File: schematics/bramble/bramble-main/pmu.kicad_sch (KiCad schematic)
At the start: 19 parts, among them J1 Conn_01x05_Pin, J7 PMU SUPPLY, J8 MAIN SUPPLY, SW1 STM_RESET, U2 STM32L031F6P6TR, U3 MCP1700x-120xxMB, Y1 Crystal

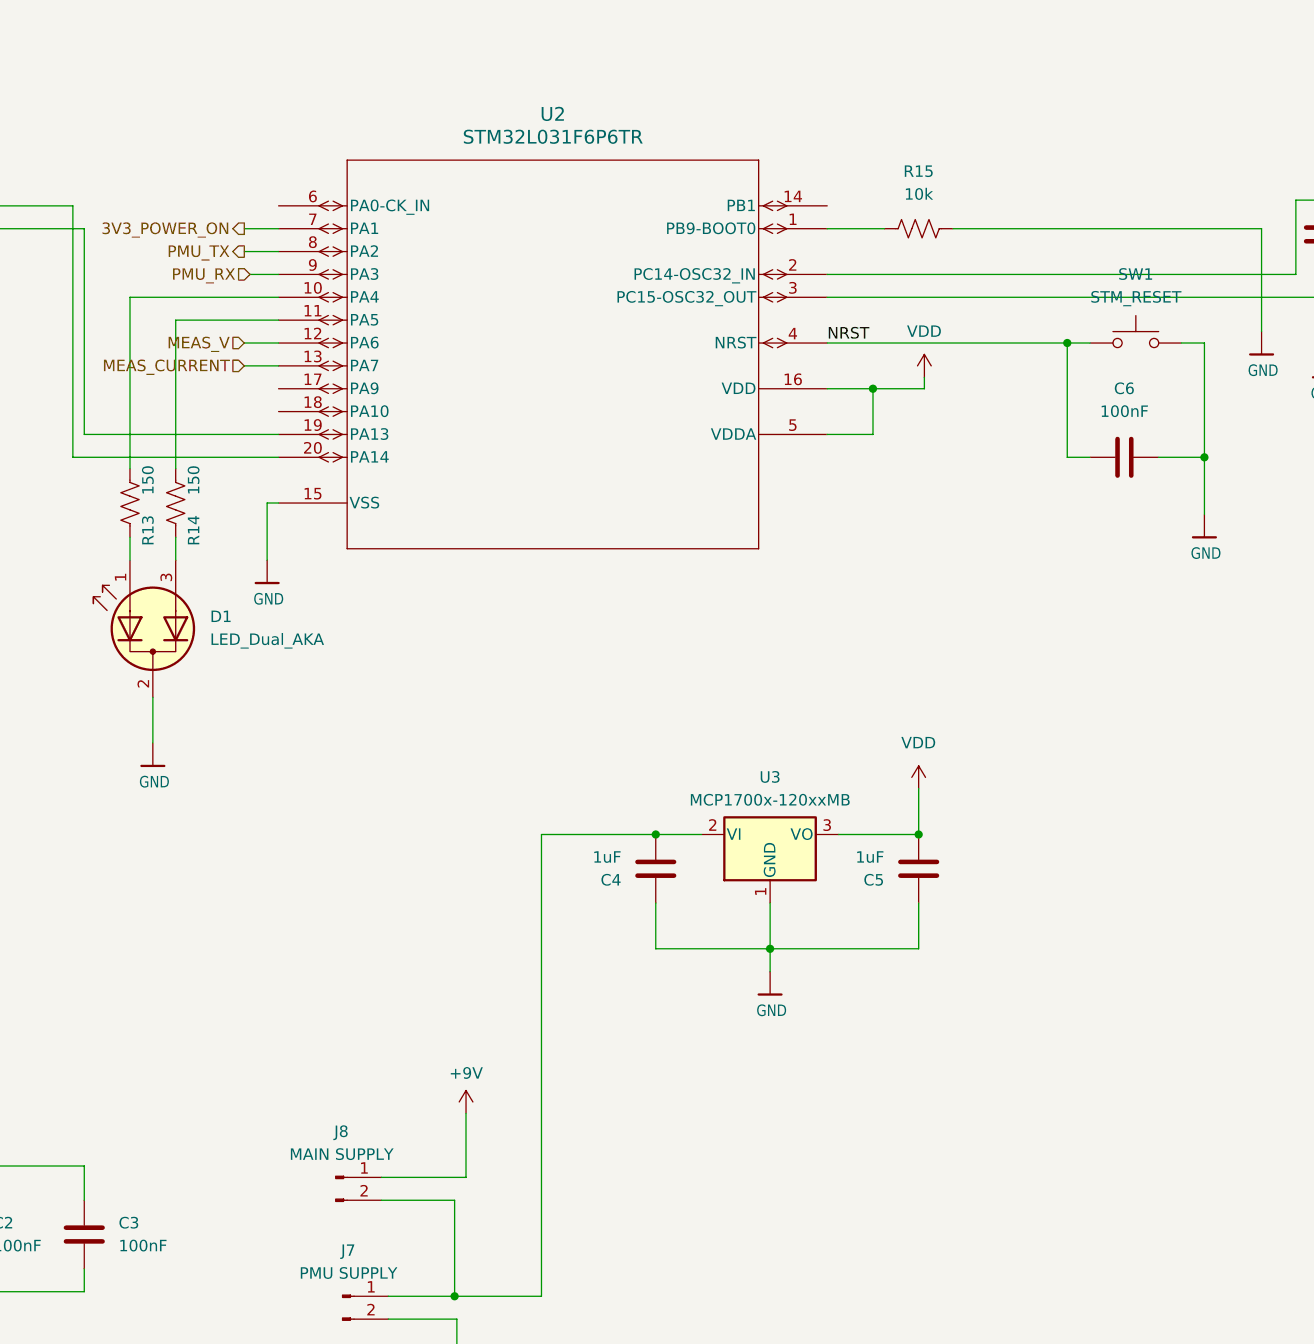
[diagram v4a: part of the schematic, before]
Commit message: Add test pads
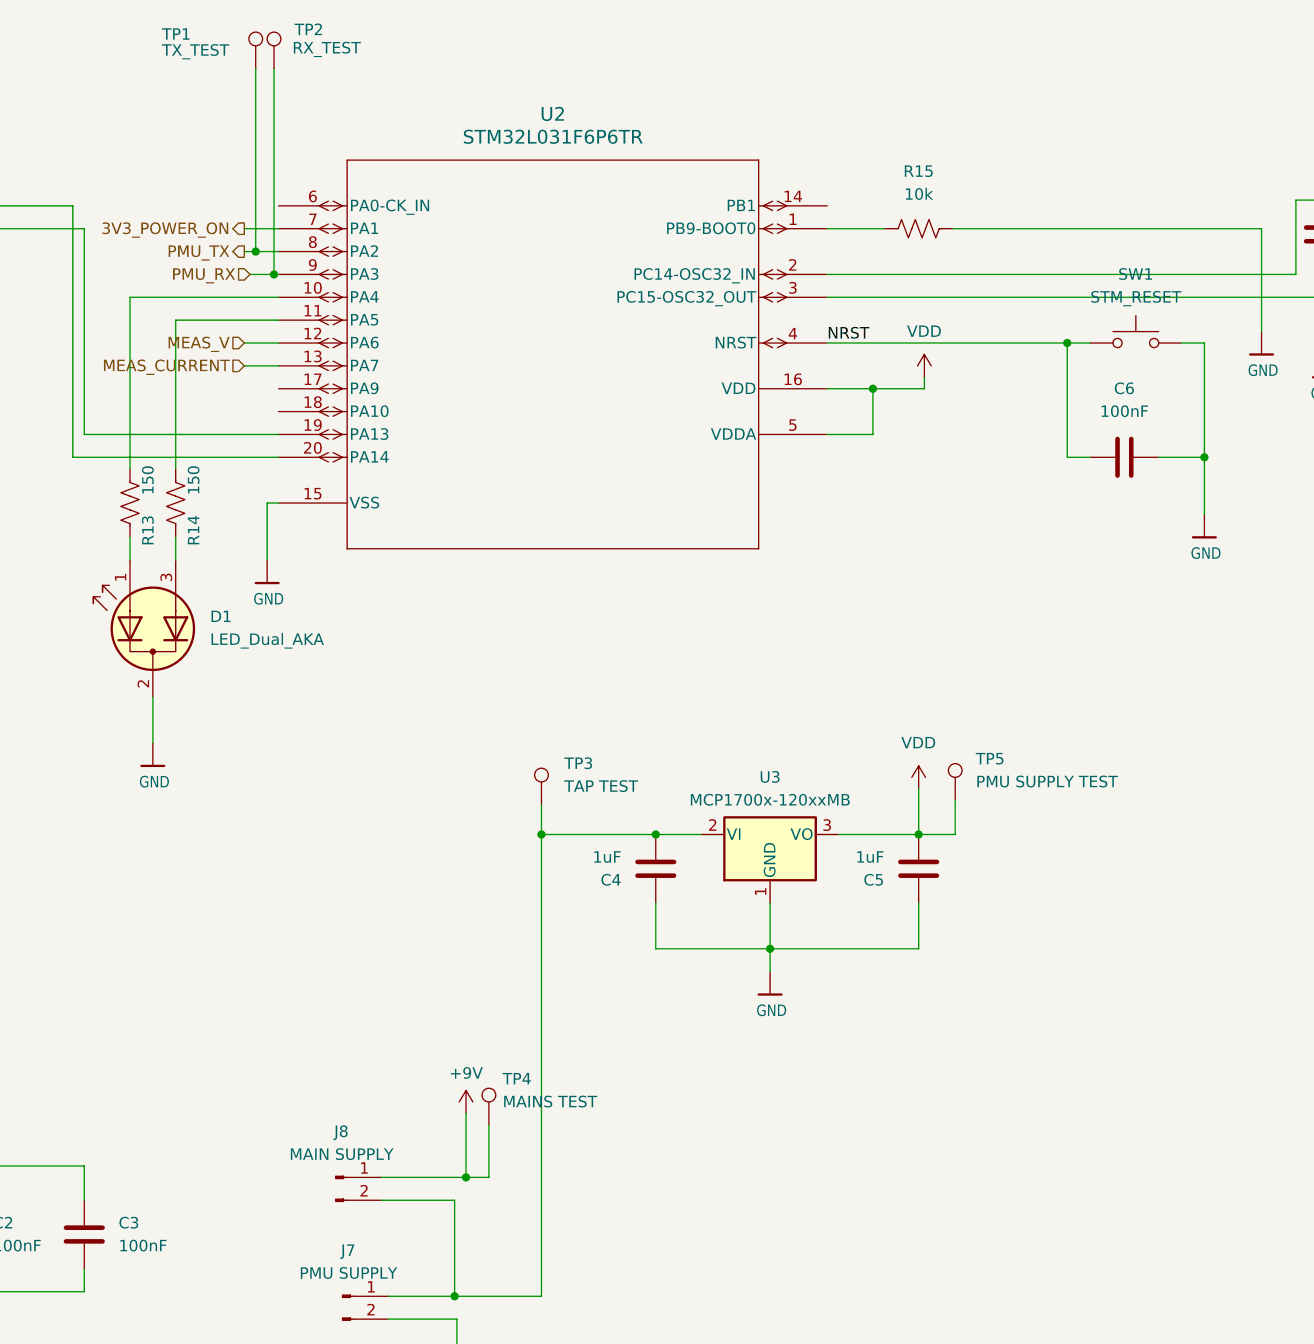
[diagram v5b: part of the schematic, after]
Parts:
- added TP1: TX_TEST, TestPoint:TestPoint_THTPad_1.5x1.5mm_Drill0.7mm, symbol Connector:TestPoint
- added TP2: RX_TEST, symbol Connector:TestPoint
- added TP3: TAP TEST, TestPoint:TestPoint_Pad_1.5x1.5mm, symbol Connector:TestPoint
- added TP4: MAINS TEST, TestPoint:TestPoint_Pad_1.5x1.5mm, symbol Connector:TestPoint
- added TP5: PMU SUPPLY TEST, TestPoint:TestPoint_Pad_1.5x1.5mm, symbol Connector:TestPoint
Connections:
- net +9V: now also TP4.1
- net PMU_RX: now also TP2.1
- net PMU_TX: now also TP1.1
- net VDD: now also TP5.1
- net at C4.2, J7.1 (Pin_1), J8.2 (Pin_2)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: now also TP3.1

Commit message: Checking in v4 schematic/board prior to attempting jlcpcb run
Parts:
- removed D1: LED_Dual_AKA, LED_THT:LED_D3.0mm-3, symbol Device:LED_Dual_AKA
- removed R13, R14: 150, Resistor_SMD:R_0805_2012Metric, symbol Device:R_US
- added J2: UART, Connector_JST:JST_SH_BM03B-SRSS-TB_1x03-1MP_P1.00mm_Vertical, symbol Connector_Generic:Conn_01x03
- added JP1: Series, TestPoint:TestPoint_2Pads_Pitch2.54mm_Drill0.8mm, symbol Jumper:Jumper_2_Open
- added JP2: Parallel 1, TestPoint:TestPoint_2Pads_Pitch2.54mm_Drill0.8mm, symbol Jumper:Jumper_2_Open
- added JP3: Parallel 2, TestPoint:TestPoint_2Pads_Pitch2.54mm_Drill0.8mm, symbol Jumper:Jumper_2_Open
- added PMU_STATUS1: WS2812B-2020, LED_SMD:LED_WS2812B-2020_PLCC4_2.0x2.0mm, symbol LED:WS2812B-2020
- added R9: 10k, Resistor_SMD:R_0805_2012Metric, symbol Device:R_US
- added SW1: STM_WAKE, Button_Switch_SMD:SW_SPST_EVQP2_MiddlePushTravel_H2.5mm, symbol Switch:SW_Push
- added U4: FM24CL16B-GTR, Package_SO:SOIC-8-1EP_3.9x4.9mm_P1.27mm_EP2.29x3mm, symbol Memory_EEPROM:24LC16
- MAIN_SUPPLY1: renamed from J8; value MAIN SUPPLY -> ~
- PMU_SUPPLY1: renamed from J7; value PMU SUPPLY -> ~
- TP2: footprint (none) -> TestPoint:TestPoint_Pad_1.5x1.5mm
- TP3: renamed from TP1; footprint TestPoint:TestPoint_THTPad_1.5x1.5mm_Drill0.7mm -> TestPoint:TestPoint_Pad_1.5x1.5mm
- renumbered C8 to C10, C1 to C3, C2 to C4, C3 to C5, C4 to C6, C5 to C7, C6 to C8, C7 to C9, R15 to R10, SW1 to SW2, TP3 to TP5, TP5 to TP6
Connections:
- net +9V: now also JP2.1 (A)
- net GND: now also J2.2 (Pin_2), PMU_STATUS1.2 (VSS), R9.1, U4.4 (GND), U4.7 (WP)
- net GNDPWR: now also JP3.2 (B)
- net VDD: now also PMU_STATUS1.4 (VDD), U4.8 (VCC)
- net at J1.2 (Pin_2), U2.20 (PA14): now also J2.1 (Pin_1)
- net at J1.3 (Pin_3), U2.19 (PA13): now also J2.3 (Pin_3)
- net at C6.2, PMU_SUPPLY1.1 (Pin_1), TP5.1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: now also JP1.2 (B), JP2.2 (B); no longer MAIN_SUPPLY1.2 (Pin_2)
- net at C10.1, U2.3 (PC15-OSC32_OUT), Y1.2: now also C9.1, U2.2 (PC14-OSC32_IN), Y1.1
- net at U2.10 (PA4): now also PMU_STATUS1.3 (DIN)
- net SCL: now reaches U2.17 (PA9)
- net SCL: now also U4.6 (SCL)
- net SDA: now reaches U2.18 (PA10)
- net SDA: now also U4.5 (SDA)
- net at U2.6 (PA0-CK_IN): now also SW1.2
- new net: R9.2, SW1.1
- new net: JP1.1 (A), JP3.1 (A), MAIN_SUPPLY1.2 (Pin_2)
- no-connect marks 0 -> 6
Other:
- note added: "STM FRAM"
- note added: "STM POWER"
- note added: "STM32"
- moved on the sheet: C10, C3, C4, C5, C6, C7, C9, MAIN_SUPPLY1, PMU_SUPPLY1, TP2, TP4, TP5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

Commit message: Update connector values and regenerate manufacturing files
Set JST PH power connector values to B2B-PH-K-S, fix reference
designator numbering, and assign remaining JLCPCB parts. Regenerated
Gerbers, BOM, and CPL for fabrication.
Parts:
- MAIN_SUPPLY1, PMU_SUPPLY1: value ~ -> B2B-PH-K-S
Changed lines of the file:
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@@
 			)
 		)
-		(property "Value" "~"
+		(property "Value" "B2B-PH-K-S"
 			(at 86.995 175.26 0)
 			(effects
@@
 		(dnp no)
 		(fields_autoplaced yes)
-		(property "Reference" "#PWR071"
+		(property "Reference" "#PWR023"
 			(at 134.62 148.59 0)
 			(effects
@@
 			(project "bramble"
 				(path "/e35d7dcf-51bd-456f-89cf-e52d660079b4/df1d8afa-9717-44ff-901e-40cae4aada91"
-					(reference "#PWR071")
+					(reference "#PWR023")
 					(unit 1)
 				)
@@
 		(dnp no)
 		(fields_autoplaced yes)
-		(property "Reference" "#PWR026"
+		(property "Reference" "#PWR027"
 			(at 215.9 80.01 0)
 			(effects
@@
 			(project ""
 				(path "/e35d7dcf-51bd-456f-89cf-e52d660079b4/df1d8afa-9717-44ff-901e-40cae4aada91"
-					(reference "#PWR026")
+					(reference "#PWR027")
 					(unit 1)
 				)
@@
 			)
 		)
-		(property "Value" "~"
+		(property "Value" "B2B-PH-K-S"
 			(at 86.995 162.56 0)
 			(effects
@@
 		(dnp no)
 		(fields_autoplaced yes)
-		(property "Reference" "#PWR027"
+		(property "Reference" "#PWR028"
 			(at 231.14 133.35 0)
 			(effects
@@
 			(project "bramble"
 				(path "/e35d7dcf-51bd-456f-89cf-e52d660079b4/df1d8afa-9717-44ff-901e-40cae4aada91"
-					(reference "#PWR027")
+					(reference "#PWR028")
 					(unit 1)
 				)
@@
 		(dnp no)
 		(fields_autoplaced yes)
-		(property "Reference" "#PWR023"
+		(property "Reference" "#PWR024"
 			(at 149.86 125.73 0)
 			(effects
@@
 			(project "bramble"
 				(path "/e35d7dcf-51bd-456f-89cf-e52d660079b4/df1d8afa-9717-44ff-901e-40cae4aada91"
-					(reference "#PWR023")
+					(reference "#PWR024")
 					(unit 1)
 				)
@@
 		(dnp no)
 		(fields_autoplaced yes)
-		(property "Reference" "#PWR024"
+		(property "Reference" "#PWR025"
 			(at 167.64 72.39 0)
 			(effects
@@
 			(project "bramble"
 				(path "/e35d7dcf-51bd-456f-89cf-e52d660079b4/df1d8afa-9717-44ff-901e-40cae4aada91"
-					(reference "#PWR024")
+					(reference "#PWR025")
 					(unit 1)
 				)
@@
 		(dnp no)
 		(fields_autoplaced yes)
-		(property "Reference" "#PWR025"
+		(property "Reference" "#PWR026"
 			(at 198.12 90.17 0)
 			(effects
@@
 			(project "bramble"
 				(path "/e35d7dcf-51bd-456f-89cf-e52d660079b4/df1d8afa-9717-44ff-901e-40cae4aada91"
-					(reference "#PWR025")
+					(reference "#PWR026")
 					(unit 1)
 				)
@@
 		(dnp no)
 		(fields_autoplaced yes)
-		(property "Reference" "#PWR028"
+		(property "Reference" "#PWR029"
 			(at 231.14 158.75 0)
 			(effects
@@
 			(project "bramble"
 				(path "/e35d7dcf-51bd-456f-89cf-e52d660079b4/df1d8afa-9717-44ff-901e-40cae4aada91"
-					(reference "#PWR028")
-					(unit 1)
-				)
+					(reference "#PWR029")
+					(unit 1)
+				)
